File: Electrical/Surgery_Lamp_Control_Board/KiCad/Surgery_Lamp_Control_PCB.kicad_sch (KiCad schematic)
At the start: 45 parts, among them J1 joint2, J2 joint3, J3 joint4, J4 Headlamp, J5 Joint 1 Encoder, J6 Joint 2 Encoder, J7 OSTVN05A150, J8 Stepper, J9 Fan, Q1 BSS138, Q2 BSS138, Q3 BSS138, Q4 BSS138, Q5 BSS138, Q6 BSS138, U1 MAX485E, U2 PCA9685PW

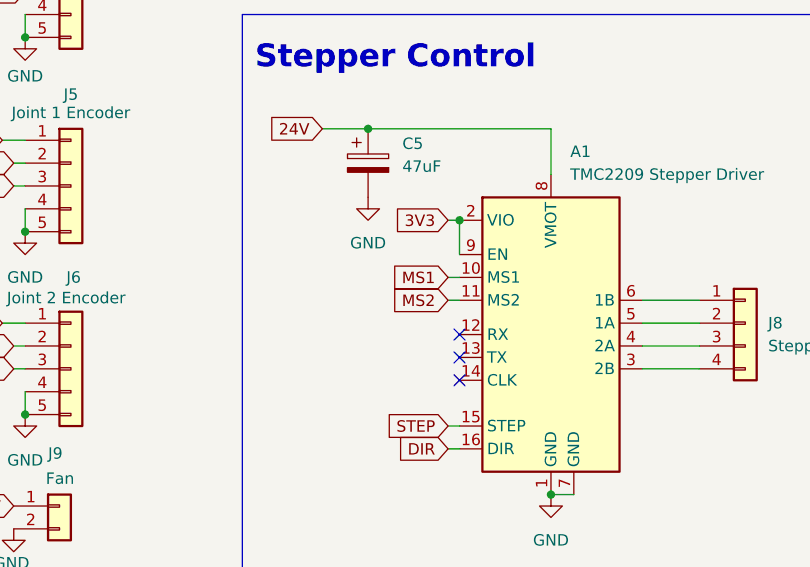
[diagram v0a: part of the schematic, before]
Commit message: Add autosave lock file for Surgery Lamp Control PCB
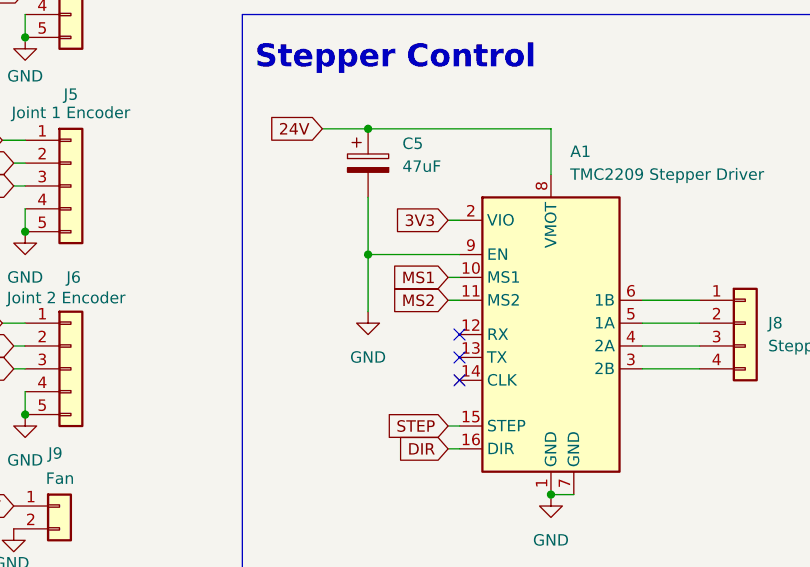
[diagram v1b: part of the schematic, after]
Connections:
- net 3V3: no longer A1.9 (EN)
- net GND: now also A1.9 (EN)
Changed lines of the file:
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@@
 	)
 	(junction
-		(at 81.28 62.23)
-		(diameter 0)
-		(color 0 0 0 0)
-	)
-	(junction
 		(at 270.51 124.46)
 		(diameter 0)
@@
 	)
 	(junction
+		(at 71.12 66.04)
+		(diameter 0)
+		(color 0 0 0 0)
+	)
+	(junction
 		(at 137.16 50.8)
 		(diameter 0)
@@
 	(wire
 		(pts
-			(xy 81.28 62.23) (xy 81.28 66.04)
-		)
-		(stroke
-			(width 0)
-			(type default)
-		)
-	)
-	(wire
-		(pts
 			(xy 30.48 73.66) (xy 33.02 73.66)
 		)
@@
 	(wire
 		(pts
+			(xy 81.28 66.04) (xy 71.12 66.04)
+		)
+		(stroke
+			(width 0)
+			(type default)
+		)
+	)
+	(wire
+		(pts
 			(xy 259.08 124.46) (xy 270.51 124.46)
 		)
@@
 	(wire
 		(pts
+			(xy 71.12 66.04) (xy 71.12 59.69)
+		)
+		(stroke
+			(width 0)
+			(type default)
+		)
+	)
+	(wire
+		(pts
 			(xy 144.78 46.99) (xy 144.78 53.34)
 		)
@@
 	(wire
 		(pts
+			(xy 71.12 66.04) (xy 71.12 72.39)
+		)
+		(stroke
+			(width 0)
+			(type default)
+		)
+	)
+	(wire
+		(pts
 			(xy 259.08 39.37) (xy 259.08 41.91)
 		)
@@
 	(symbol
 		(lib_id "power:GND")
-		(at 71.12 59.69 0)
+		(at 71.12 72.39 0)
 		(unit 1)
 		(exclude_from_sim no)
@@
 		(fields_autoplaced yes)
 		(property "Reference" "#PWR010"
-			(at 71.12 66.04 0)
+			(at 71.12 78.74 0)
 			(effects
 				(font
@@
 		)
 		(property "Value" "GND"
-			(at 71.12 64.77 0)
+			(at 71.12 77.47 0)
 			(effects
 				(font
@@
 		)
 		(property "Footprint" ""
-			(at 71.12 59.69 0)
+			(at 71.12 72.39 0)
 			(effects
 				(font
@@
 		)
 		(property "Datasheet" ""
-			(at 71.12 59.69 0)
+			(at 71.12 72.39 0)
 			(effects
 				(font
@@
 		)
 		(property "Description" "Power symbol creates a global label with name \"GND\" , ground"
-			(at 71.12 59.69 0)
+			(at 71.12 72.39 0)
 			(effects
 				(font
